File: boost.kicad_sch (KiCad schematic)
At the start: 25 parts, among them Q5 BSC059N04LS6, Q6 BSC059N04LS6, U7 LM5123-Q1

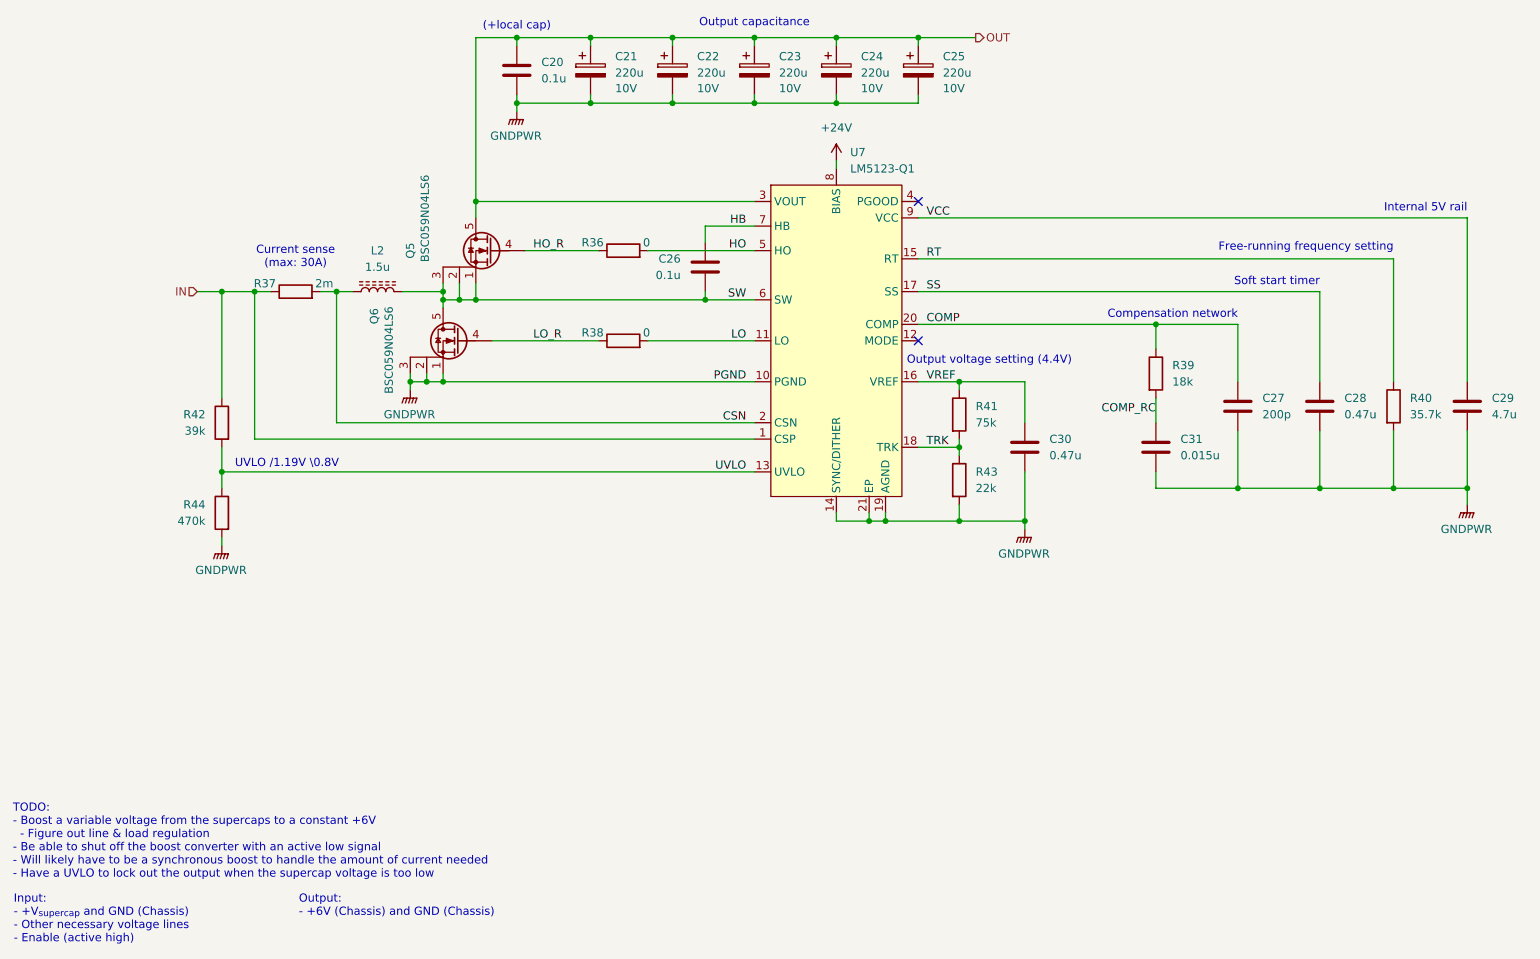
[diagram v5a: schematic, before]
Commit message: Specc'd all components + started creating rev 1b boards
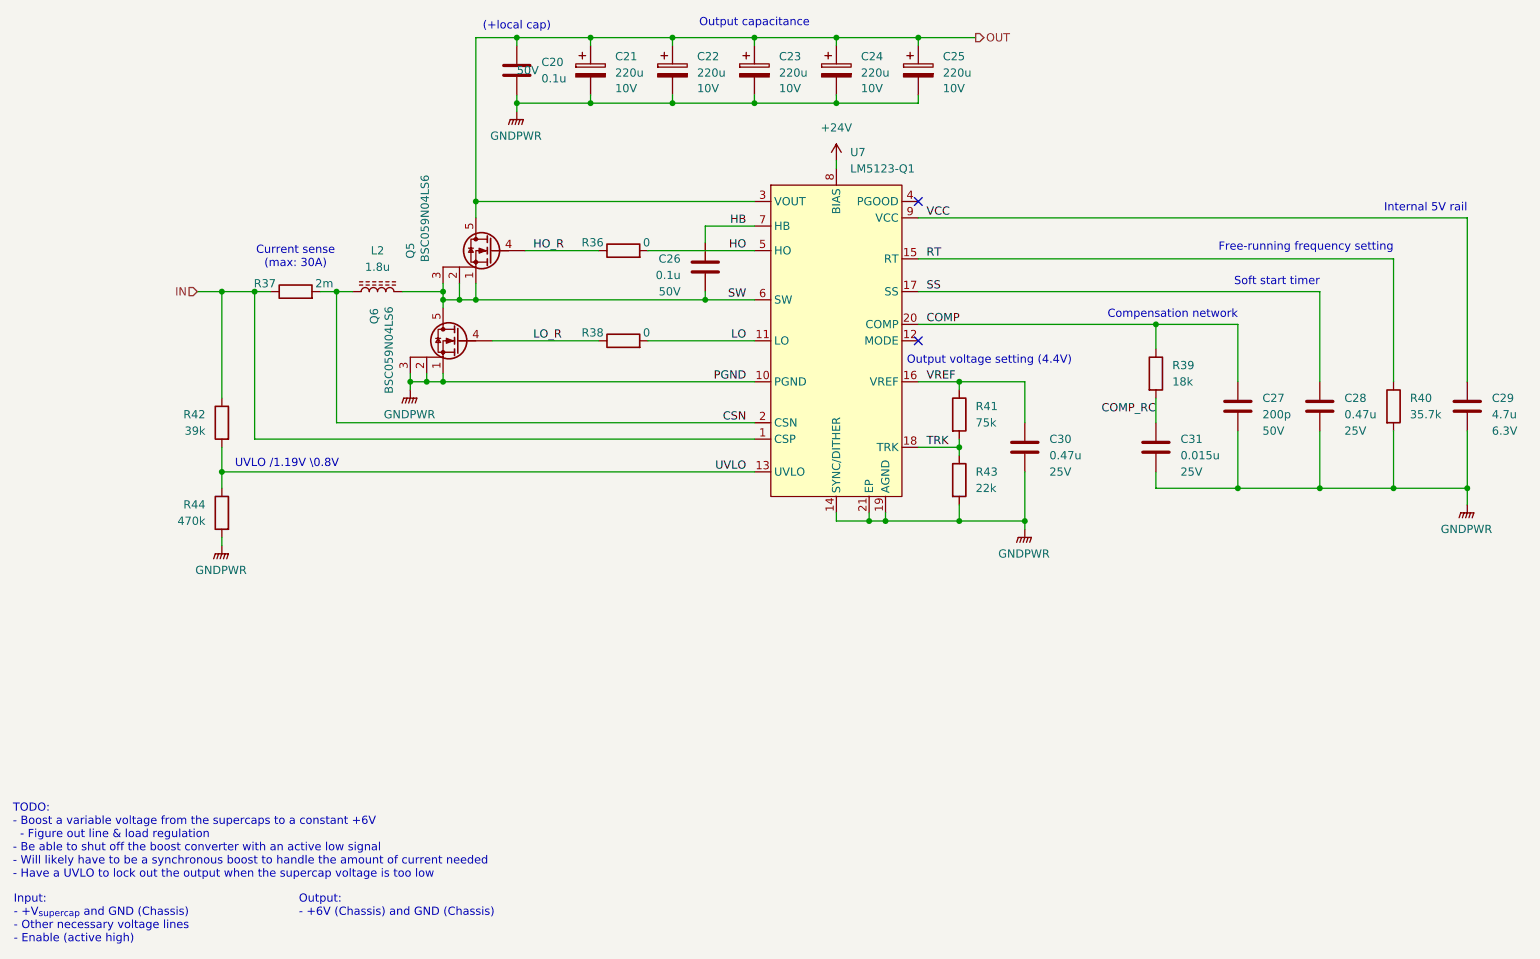
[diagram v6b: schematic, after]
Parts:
- C20, C26: Mouser Part Number (none) -> 581-KGM15BR71H104JT; Voltage Rating (none) -> 50V
- C27: Mouser Part Number (none) -> 187-CL10C201JB8NNNC; Voltage Rating (none) -> 50V
- C28, C30: Mouser Part Number (none) -> 710-885012106020; Voltage Rating (none) -> 25V
- C29: Mouser Part Number (none) -> 187-CL10A475KQ8NNWC; Voltage Rating (none) -> 6.3V
- C31: Mouser Part Number (none) -> 77-VJ0603Y153KXXCBC; Voltage Rating (none) -> 25V
- L2: value 1.5u -> 1.8u
- R36, R38: Mouser Part Number (none) -> 660-RK73Z1JTTDD
- R39: Mouser Part Number (none) -> 603-RT0603FRE1318KL
- R40: Mouser Part Number (none) -> 603-RC0603FR-0735K7L
- R41: Mouser Part Number (none) -> 03-AC0603FR-1075KL
- R42: Mouser Part Number (none) -> 603-RC0603FR-1339KL
- R43: Mouser Part Number (none) -> 71-CRCW0603-22K-E3
- R44: Mouser Part Number 603-RT0603BRD07280KL -> 660-RN73R1JTD4703B25
- U7: Mouser Part Number (none) -> 595-LM51231QRGRRQ1
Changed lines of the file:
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@@
 			)
 		)
-		(property "Mouser Part Number" "603-RT0603BRD07280KL"
+		(property "Mouser Part Number" "660-RN73R1JTD4703B25"
 			(at 52.07 124.46 0)
 			(effects
@@
 			)
 		)
+		(property "Mouser Part Number" "187-CL10A475KQ8NNWC"
+			(at 245.11 107.95 0)
+			(effects
+				(font
+					(size 1.27 1.27)
+				)
+				(hide yes)
+			)
+		)
+		(property "Voltage Rating" "6.3V"
+			(at 248.92 111.76 0)
+			(effects
+				(font
+					(size 1.27 1.27)
+				)
+				(justify right)
+			)
+		)
 		(pin "1"
 		)
@@
 			)
 		)
+		(property "Mouser Part Number" "603-RC0603FR-0735K7L"
+			(at 233.68 107.95 0)
+			(effects
+				(font
+					(size 1.27 1.27)
+				)
+				(hide yes)
+			)
+		)
 		(pin "2"
 		)
@@
 			)
 		)
-		(property "Datasheet" "~"
+		(property "Datasheet" "https://www.mouser.com/datasheet/2/585/MLCC-1837944.pdf"
 			(at 209.55 107.95 0)
 			(effects
@@
 				)
 				(hide yes)
+			)
+		)
+		(property "Mouser Part Number" "187-CL10C201JB8NNNC"
+			(at 209.55 107.95 0)
+			(effects
+				(font
+					(size 1.27 1.27)
+				)
+				(hide yes)
+			)
+		)
+		(property "Voltage Rating" "50V"
+			(at 213.36 111.76 0)
+			(effects
+				(font
+					(size 1.27 1.27)
+				)
+				(justify right)
 			)
 		)
@@
 			)
 		)
+		(property "Mouser Part Number" "603-RC0603FR-1339KL"
+			(at 52.07 110.49 0)
+			(effects
+				(font
+					(size 1.27 1.27)
+				)
+				(hide yes)
+			)
+		)
 		(pin "2"
 		)
@@
 			)
 		)
+		(property "Mouser Part Number" "660-RK73Z1JTTDD"
+			(at 114.3 83.82 0)
+			(effects
+				(font
+					(size 1.27 1.27)
+				)
+				(hide yes)
+			)
+		)
 		(pin "2"
 		)
@@
 					(size 1.27 1.27)
 				)
+			)
+		)
+		(property "Mouser Part Number" "660-RK73Z1JTTDD"
+			(at 114.3 97.79 0)
+			(effects
+				(font
+					(size 1.27 1.27)
+				)
+				(hide yes)
 			)
 		)
@@
 			)
 		)
+		(property "Mouser Part Number" "595-LM51231QRGRRQ1"
+			(at 147.32 73.66 0)
+			(effects
+				(font
+					(size 1.27 1.27)
+				)
+				(hide yes)
+			)
+		)
 		(pin "19"
 		)
@@
 			)
 		)
+		(property "Mouser Part Number" "710-885012106020"
+			(at 222.25 107.95 0)
+			(effects
+				(font
+					(size 1.27 1.27)
+				)
+				(hide yes)
+			)
+		)
+		(property "Voltage Rating" "25V"
+			(at 226.06 111.76 0)
+			(effects
+				(font
+					(size 1.27 1.27)
+				)
+				(justify right)
+			)
+		)
 		(pin "1"
 		)
@@
 			)
 		)
+		(property "Mouser Part Number" "77-VJ0603Y153KXXCBC"
+			(at 196.85 114.3 0)
+			(effects
+				(font
+					(size 1.27 1.27)
+				)
+				(hide yes)
+			)
+		)
+		(property "Voltage Rating" "25V"
+			(at 200.66 118.11 0)
+			(effects
+				(font
+					(size 1.27 1.27)
+				)
+				(justify right)
+			)
+		)
 		(pin "1"
 		)
@@
 			)
 		)
+		(property "Mouser Part Number" "71-CRCW0603-22K-E3"
+			(at 166.37 119.38 0)
+			(effects
+				(font
+					(size 1.27 1.27)
+				)
+				(hide yes)
+			)
+		)
 		(pin "2"
 		)
@@
 		)
 		(property "Description" "Resistor"
+			(at 196.85 102.87 0)
+			(effects
+				(font
+					(size 1.27 1.27)
+				)
+				(hide yes)
+			)
+		)
+		(property "Mouser Part Number" "603-RT0603FRE1318KL"
 			(at 196.85 102.87 0)
 			(effects
@@
 			)
 		)
+		(property "Mouser Part Number" "710-885012106020"
+			(at 176.53 114.3 0)
+			(effects
+				(font
+					(size 1.27 1.27)
+				)
+				(hide yes)
+			)
+		)
+		(property "Voltage Rating" "25V"
+			(at 180.34 118.11 0)
+			(effects
+				(font
+					(size 1.27 1.27)
+				)
+				(justify right)
+			)
+		)
 		(pin "1"
 		)
@@
 			)
 		)
-		(property "Value" "1.5u"
+		(property "Value" "1.8u"
 			(at 76.2 86.36 90)
 			(effects
@@
 			)
 		)
-		(property "Datasheet" "~"
+		(property "Datasheet" "https://www.mouser.com/datasheet/2/40/KGM_X7R-3223212.pdf"
 			(at 127 86.36 0)
 			(effects
@@
 				)
 				(hide yes)
+			)
+		)
+		(property "Mouser Part Number" "581-KGM15BR71H104JT"
+			(at 127 86.36 0)
+			(effects
+				(font
+					(size 1.27 1.27)
+				)
+				(hide yes)
+			)
+		)
+		(property "Voltage Rating" "50V"
+			(at 123.19 90.17 0)
+			(effects
+				(font
+					(size 1.27 1.27)
+				)
+				(justify right)
 			)
 		)
@@
 			)
 		)
+		(property "Mouser Part Number" "03-AC0603FR-1075KL"
+			(at 166.37 109.22 0)
+			(effects
+				(font
+					(size 1.27 1.27)
+				)
+				(hide yes)
+			)
+		)
 		(pin "2"
 		)
@@
 			)
 		)
-		(property "Datasheet" "~"
+		(property "Datasheet" "https://www.mouser.com/datasheet/2/40/KGM_X7R-3223212.pdf"
 			(at 97.79 55.88 0)
 			(effects
@@
 			)
 		)
+		(property "Mouser Part Number" "581-KGM15BR71H104JT"
+			(at 97.79 55.88 0)
+			(effects
+				(font
+					(size 1.27 1.27)
+				)
+				(hide yes)
+			)
+		)
+		(property "Voltage Rating" "50V"
+			(at 97.79 55.88 0)
+			(effects
+				(font
+					(size 1.27 1.27)
+				)
+				(justify right)
+			)
+		)

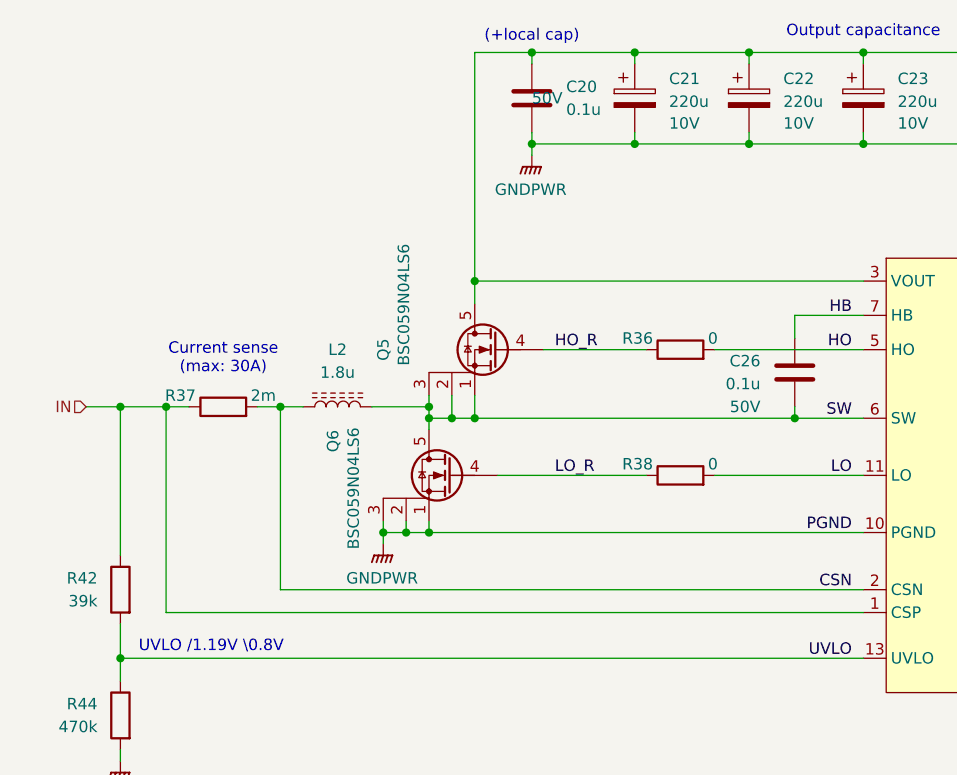
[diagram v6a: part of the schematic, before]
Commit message: Add test points to all subsheets
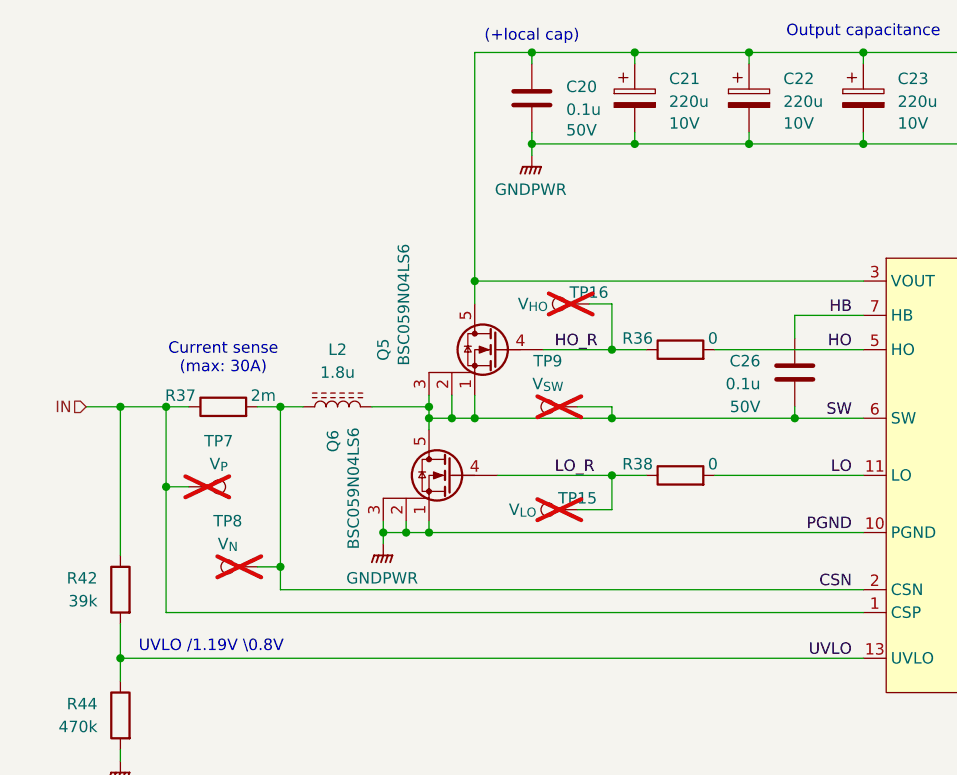
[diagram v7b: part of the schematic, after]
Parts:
- added TP15: V_{LO}, TestPoint:TestPoint_Bridge_Pitch2.0mm_Drill0.7mm, symbol Connector:TestPoint
- added TP16: V_{HO}, TestPoint:TestPoint_Bridge_Pitch2.0mm_Drill0.7mm, symbol Connector:TestPoint
- added TP7: V_{P}, TestPoint:TestPoint_Bridge_Pitch2.0mm_Drill0.7mm, symbol Connector:TestPoint
- added TP8: V_{N}, TestPoint:TestPoint_Bridge_Pitch2.0mm_Drill0.7mm, symbol Connector:TestPoint
- added TP9: V_{SW}, TestPoint:TestPoint_Bridge_Pitch2.0mm_Drill0.7mm, symbol Connector:TestPoint
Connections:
- net CSN: now also TP8.1
- net HO_R: now also TP16.1
- net IN: now also TP7.1
- net LO_R: now also TP15.1
- net SW: now also TP9.1

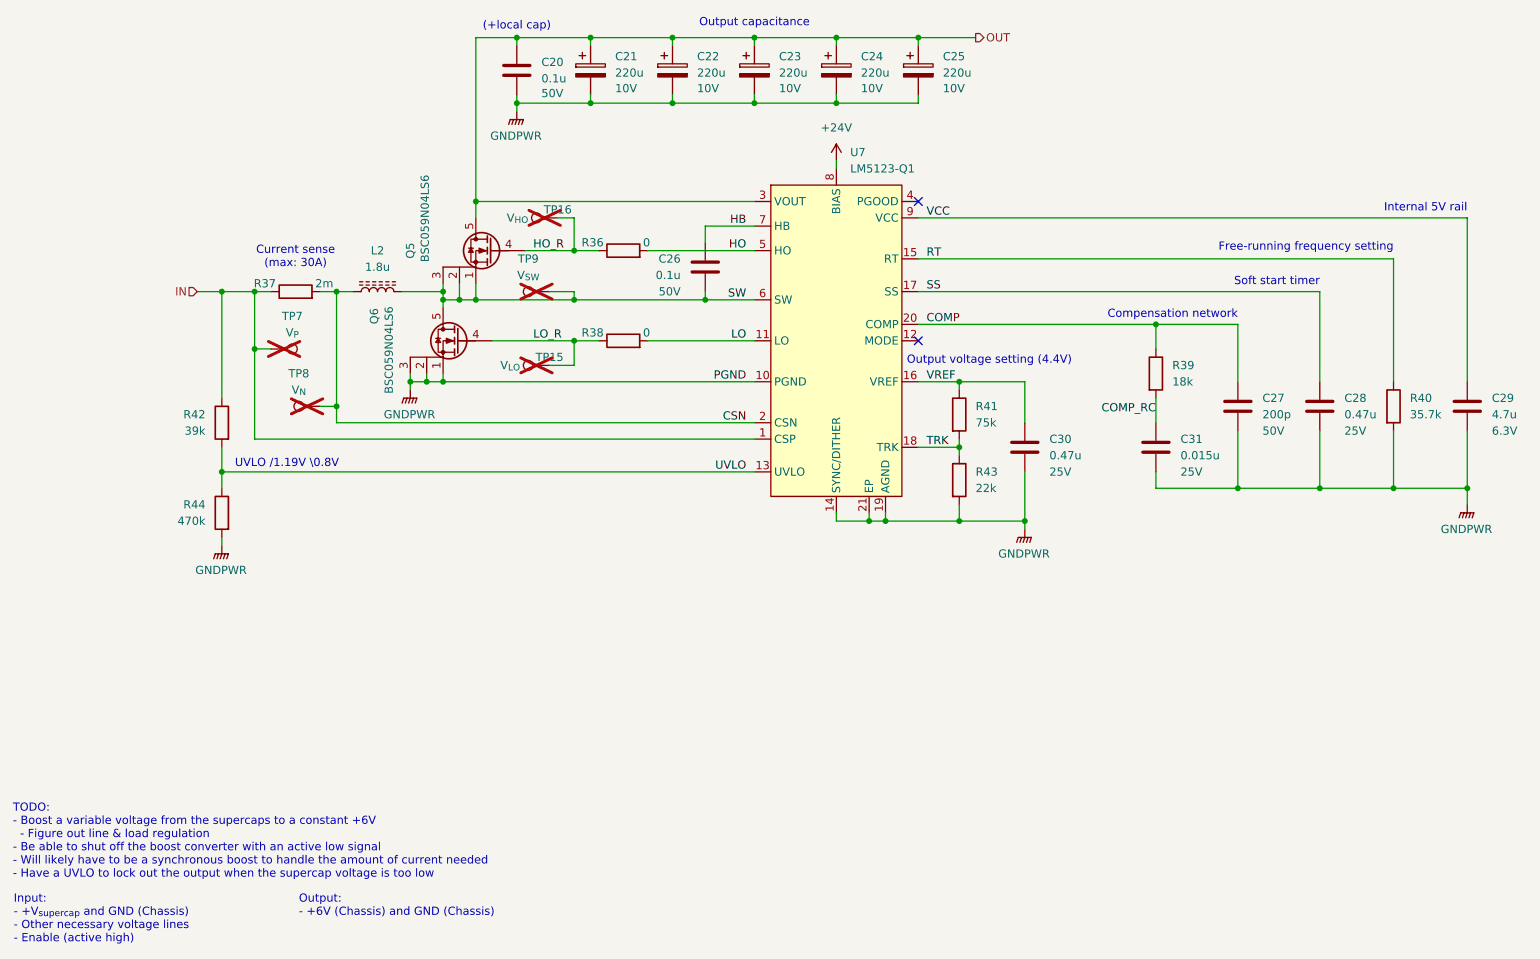
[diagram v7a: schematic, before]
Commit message: Renumbered components for rev 1b layout
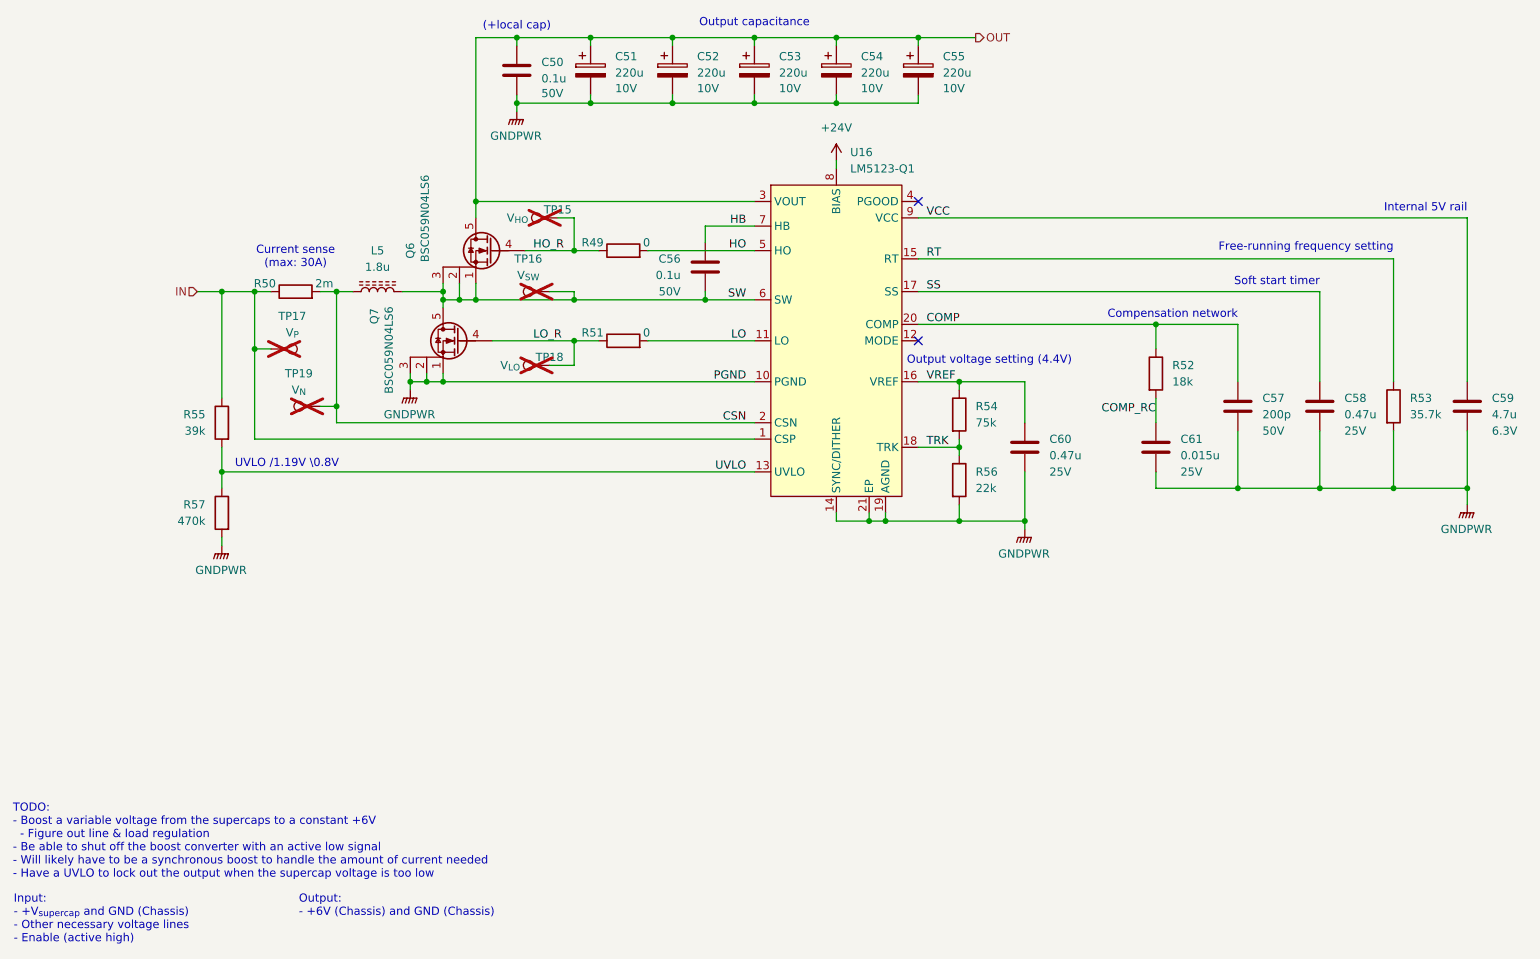
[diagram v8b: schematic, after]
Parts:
- renumbered C20 to C50, C21 to C51, C22 to C52, C23 to C53, C24 to C54, C25 to C55, C26 to C56, C27 to C57, C28 to C58, C29 to C59, C30 to C60, C31 to C61, L2 to L5, Q5 to Q6, Q6 to Q7, R36 to R49, R37 to R50, R38 to R51, R39 to R52, R40 to R53, R41 to R54, R42 to R55, R43 to R56, R44 to R57, TP16 to TP15, TP9 to TP16, TP7 to TP17, TP15 to TP18, TP8 to TP19, U7 to U16
